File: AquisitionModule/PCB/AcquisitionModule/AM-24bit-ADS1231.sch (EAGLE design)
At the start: 4 parts, among them U1 ADS1231ID

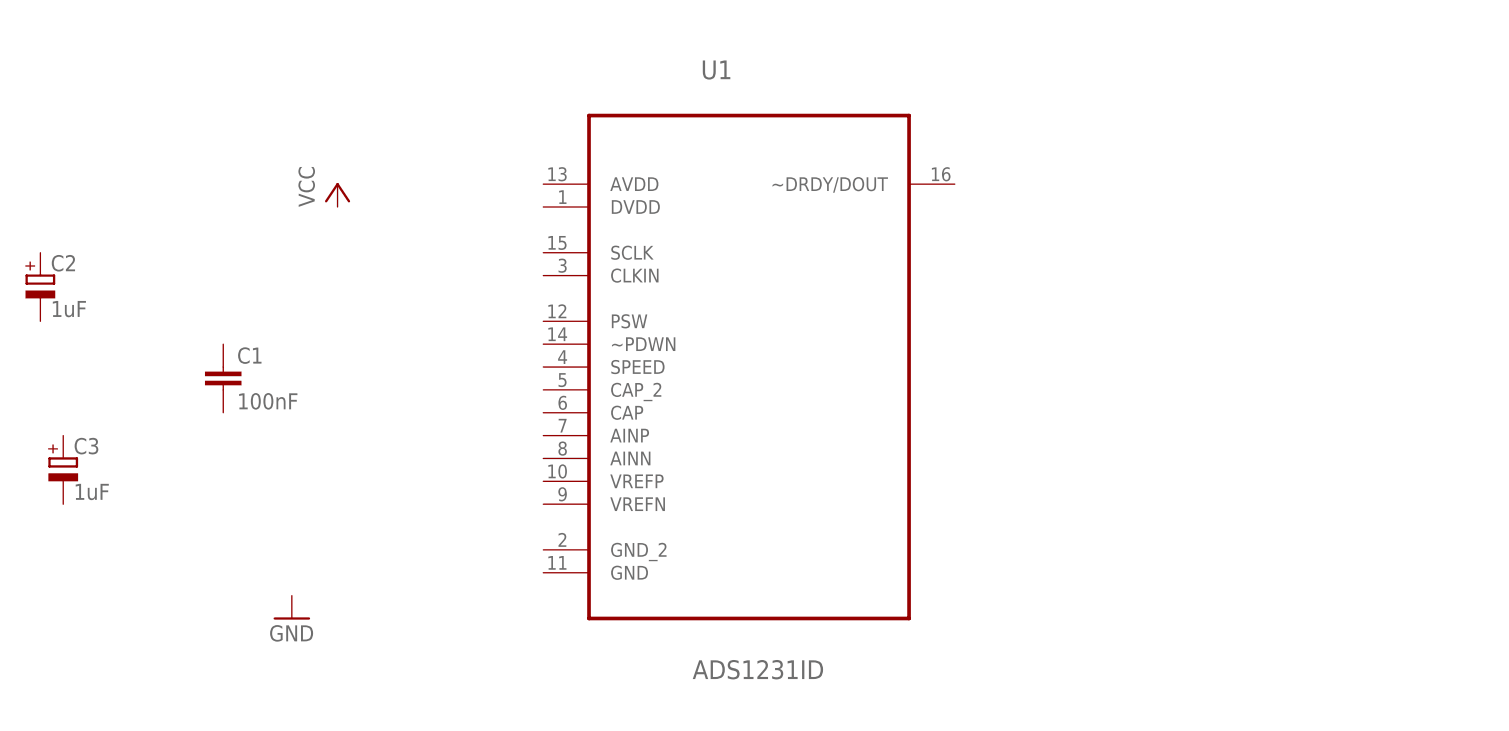
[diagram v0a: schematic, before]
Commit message: Wiring components in Acquisition Module schematic
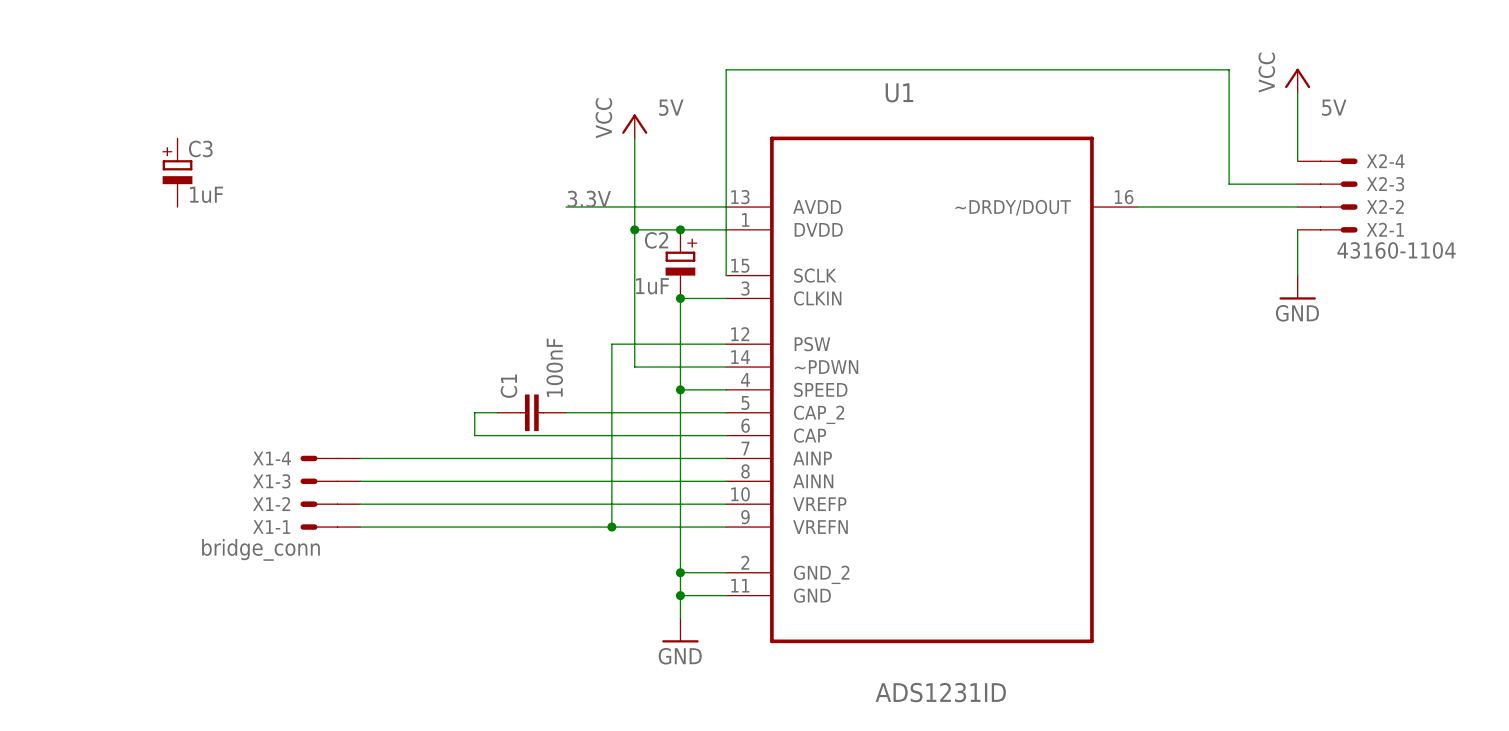
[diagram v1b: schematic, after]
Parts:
- added X1: bridge_conn, con-molex:43160-1104
- added X2: 43160-1104, con-molex:43160-1104
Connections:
- new net 3.3V: U1.AVDD
- new net 5V: C2.+, U1.DVDD, U1.~PDWN, X2-4.S@1
- new net GND: C2.-, U1.CLKIN, U1.GND, U1.GND_2, U1.SPEED, X2-1.S@1
- new net N$1: C1.2, U1.CAP_2
- new net N$2: C1.1, U1.CAP
- new net N$3: U1.PSW, U1.VREFN, X1-1.S@1
- new net N$4: U1.AINP, X1-4.S@1
- new net N$5: U1.AINN, X1-3.S@1
- new net N$6: U1.VREFP, X1-2.S@1
- new net N$7: U1.SCLK, X2-3.S@1
- new net N$8: U1.~DRDY/DOUT, X2-2.S@1
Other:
- moved on the sheet: C1, C2, C3, U1
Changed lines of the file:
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@@
 <part name="C2" library="rcl" deviceset="CPOL-EU" device="140CLH-0810" value="1uF"/>
 <part name="C3" library="rcl" deviceset="CPOL-EU" device="140CLH-0810" value="1uF"/>
-<part name="P+1" library="supply1" deviceset="VCC" device=""/>
+<part name="5V" library="supply1" deviceset="VCC" device=""/>
 <part name="GND1" library="supply1" deviceset="GND" device=""/>
+<part name="X1" library="con-molex" deviceset="43160-*04" device="" technology="11" value="bridge_conn"/>
+<part name="X2" library="con-molex" deviceset="43160-*04" device="" technology="11"/>
+<part name="5V1" library="supply1" deviceset="VCC" device=""/>
+<part name="GND2" library="supply1" deviceset="GND" device=""/>
 </parts>
 <sheets>
@@
 <instances>
 <instance part="FRAME1" gate="G$1" x="0" y="0"/>
-<instance part="U1" gate="A" x="119.38" y="96.52"/>
-<instance part="C1" gate="G$1" x="60.96" y="93.98"/>
-<instance part="C2" gate="G$1" x="40.64" y="104.14"/>
-<instance part="C3" gate="G$1" x="43.18" y="83.82"/>
-<instance part="P+1" gate="VCC" x="73.66" y="114.3"/>
-<instance part="GND1" gate="1" x="68.58" y="66.04"/>
+<instance part="U1" gate="A" x="139.7" y="93.98"/>
+<instance part="C1" gate="G$1" x="93.98" y="88.9" rot="R90"/>
+<instance part="C2" gate="G$1" x="111.76" y="106.68" rot="MR0"/>
+<instance part="C3" gate="G$1" x="55.88" y="116.84"/>
+<instance part="5V" gate="VCC" x="106.68" y="121.92"/>
+<instance part="GND1" gate="1" x="111.76" y="63.5"/>
+<instance part="X1" gate="-1" x="71.12" y="76.2" rot="R180"/>
+<instance part="X1" gate="-2" x="71.12" y="78.74" rot="R180"/>
+<instance part="X1" gate="-3" x="71.12" y="81.28" rot="R180"/>
+<instance part="X1" gate="-4" x="71.12" y="83.82" rot="R180"/>
+<instance part="X2" gate="-1" x="185.42" y="109.22" rot="MR180"/>
+<instance part="X2" gate="-2" x="185.42" y="111.76" rot="MR180"/>
+<instance part="X2" gate="-3" x="185.42" y="114.3" rot="MR180"/>
+<instance part="X2" gate="-4" x="185.42" y="116.84" rot="MR180"/>
+<instance part="5V1" gate="VCC" x="180.34" y="127"/>
+<instance part="GND2" gate="1" x="180.34" y="101.6"/>
 </instances>
 <busses>
 </busses>
 <nets>
+<net name="GND" class="0">
+<segment>
+<pinref part="U1" gate="A" pin="GND"/>
+<pinref part="GND1" gate="1" pin="GND"/>
+<wire x1="116.84" y1="68.58" x2="111.76" y2="68.58" width="0.1524" layer="91"/>
+<wire x1="111.76" y1="68.58" x2="111.76" y2="66.04" width="0.1524" layer="91"/>
+<pinref part="U1" gate="A" pin="GND_2"/>
+<wire x1="116.84" y1="71.12" x2="111.76" y2="71.12" width="0.1524" layer="91"/>
+<wire x1="111.76" y1="71.12" x2="111.76" y2="68.58" width="0.1524" layer="91"/>
+<junction x="111.76" y="68.58"/>
+<pinref part="U1" gate="A" pin="SPEED"/>
+<wire x1="116.84" y1="91.44" x2="111.76" y2="91.44" width="0.1524" layer="91"/>
+<wire x1="111.76" y1="91.44" x2="111.76" y2="71.12" width="0.1524" layer="91"/>
+<junction x="111.76" y="71.12"/>
+<junction x="111.76" y="91.44"/>
+<pinref part="U1" gate="A" pin="CLKIN"/>
+<wire x1="116.84" y1="101.6" x2="111.76" y2="101.6" width="0.1524" layer="91"/>
+<wire x1="111.76" y1="101.6" x2="111.76" y2="91.44" width="0.1524" layer="91"/>
+<pinref part="C2" gate="G$1" pin="-"/>
+<junction x="111.76" y="101.6"/>
+</segment>
+<segment>
+<pinref part="X2" gate="-1" pin="S@1"/>
+<pinref part="GND2" gate="1" pin="GND"/>
+<wire x1="180.34" y1="109.22" x2="180.34" y2="104.14" width="0.1524" layer="91"/>
+</segment>
+</net>
+<net name="N$1" class="0">
+<segment>
+<pinref part="U1" gate="A" pin="CAP_2"/>
+<pinref part="C1" gate="G$1" pin="2"/>
+<wire x1="116.84" y1="88.9" x2="99.06" y2="88.9" width="0.1524" layer="91"/>
+</segment>
+</net>
+<net name="N$2" class="0">
+<segment>
+<pinref part="C1" gate="G$1" pin="1"/>
+<wire x1="91.44" y1="88.9" x2="88.9" y2="88.9" width="0.1524" layer="91"/>
+<wire x1="88.9" y1="88.9" x2="88.9" y2="86.36" width="0.1524" layer="91"/>
+<pinref part="U1" gate="A" pin="CAP"/>
+<wire x1="88.9" y1="86.36" x2="116.84" y2="86.36" width="0.1524" layer="91"/>
+</segment>
+</net>
+<net name="5V" class="0">
+<segment>
+<pinref part="U1" gate="A" pin="DVDD"/>
+<pinref part="5V" gate="VCC" pin="VCC"/>
+<wire x1="116.84" y1="109.22" x2="111.76" y2="109.22" width="0.1524" layer="91"/>
+<wire x1="111.76" y1="109.22" x2="106.68" y2="109.22" width="0.1524" layer="91"/>
+<wire x1="106.68" y1="109.22" x2="106.68" y2="119.38" width="0.1524" layer="91"/>
+<label x="109.22" y="121.92" size="1.778" layer="95"/>
+<pinref part="U1" gate="A" pin="~PDWN"/>
+<wire x1="116.84" y1="93.98" x2="106.68" y2="93.98" width="0.1524" layer="91"/>
+<wire x1="106.68" y1="93.98" x2="106.68" y2="109.22" width="0.1524" layer="91"/>
+<junction x="106.68" y="109.22"/>
+<pinref part="C2" gate="G$1" pin="+"/>
+<junction x="111.76" y="109.22"/>
+</segment>
+<segment>
+<pinref part="X2" gate="-4" pin="S@1"/>
+<pinref part="5V1" gate="VCC" pin="VCC"/>
+<wire x1="180.34" y1="116.84" x2="180.34" y2="124.46" width="0.1524" layer="91"/>
+<label x="182.88" y="121.92" size="1.778" layer="95"/>
+</segment>
+</net>
+<net name="3.3V" class="0">
+<segment>
+<pinref part="U1" gate="A" pin="AVDD"/>
+<wire x1="116.84" y1="111.76" x2="99.06" y2="111.76" width="0.1524" layer="91"/>
+<label x="99.06" y="111.76" size="1.778" layer="95"/>
+</segment>
+</net>
+<net name="N$3" class="0">
+<segment>
+<pinref part="U1" gate="A" pin="PSW"/>
+<wire x1="116.84" y1="96.52" x2="104.14" y2="96.52" width="0.1524" layer="91"/>
+<wire x1="104.14" y1="96.52" x2="104.14" y2="76.2" width="0.1524" layer="91"/>
+<pinref part="U1" gate="A" pin="VREFN"/>
+<wire x1="104.14" y1="76.2" x2="116.84" y2="76.2" width="0.1524" layer="91"/>
+<pinref part="X1" gate="-1" pin="S@1"/>
+<wire x1="104.14" y1="76.2" x2="76.2" y2="76.2" width="0.1524" layer="91"/>
+<junction x="104.14" y="76.2"/>
+</segment>
+</net>
+<net name="N$4" class="0">
+<segment>
+<pinref part="U1" gate="A" pin="AINP"/>
+<pinref part="X1" gate="-4" pin="S@1"/>
+<wire x1="116.84" y1="83.82" x2="76.2" y2="83.82" width="0.1524" layer="91"/>
+</segment>
+</net>
+<net name="N$5" class="0">
+<segment>
+<pinref part="U1" gate="A" pin="AINN"/>
+<pinref part="X1" gate="-3" pin="S@1"/>
+<wire x1="116.84" y1="81.28" x2="76.2" y2="81.28" width="0.1524" layer="91"/>
+</segment>
+</net>
+<net name="N$6" class="0">
+<segment>
+<pinref part="U1" gate="A" pin="VREFP"/>
+<pinref part="X1" gate="-2" pin="S@1"/>
+<wire x1="116.84" y1="78.74" x2="76.2" y2="78.74" width="0.1524" layer="91"/>
+</segment>
+</net>
+<net name="N$7" class="0">
+<segment>
+<pinref part="U1" gate="A" pin="SCLK"/>
+<wire x1="116.84" y1="104.14" x2="116.84" y2="127" width="0.1524" layer="91"/>
+<wire x1="116.84" y1="127" x2="172.72" y2="127" width="0.1524" layer="91"/>
+<wire x1="172.72" y1="127" x2="172.72" y2="114.3" width="0.1524" layer="91"/>
+<pinref part="X2" gate="-3" pin="S@1"/>
+<wire x1="172.72" y1="114.3" x2="180.34" y2="114.3" width="0.1524" layer="91"/>
+</segment>
+</net>
+<net name="N$8" class="0">
+<segment>
+<pinref part="U1" gate="A" pin="~DRDY/DOUT"/>
+<wire x1="162.56" y1="111.76" x2="180.34" y2="111.76" width="0.1524" layer="91"/>
+<pinref part="X2" gate="-2" pin="S@1"/>
+</segment>
+</net>
 </nets>
 </sheet>

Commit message: Added reference voltage (2.5V) in the circuit
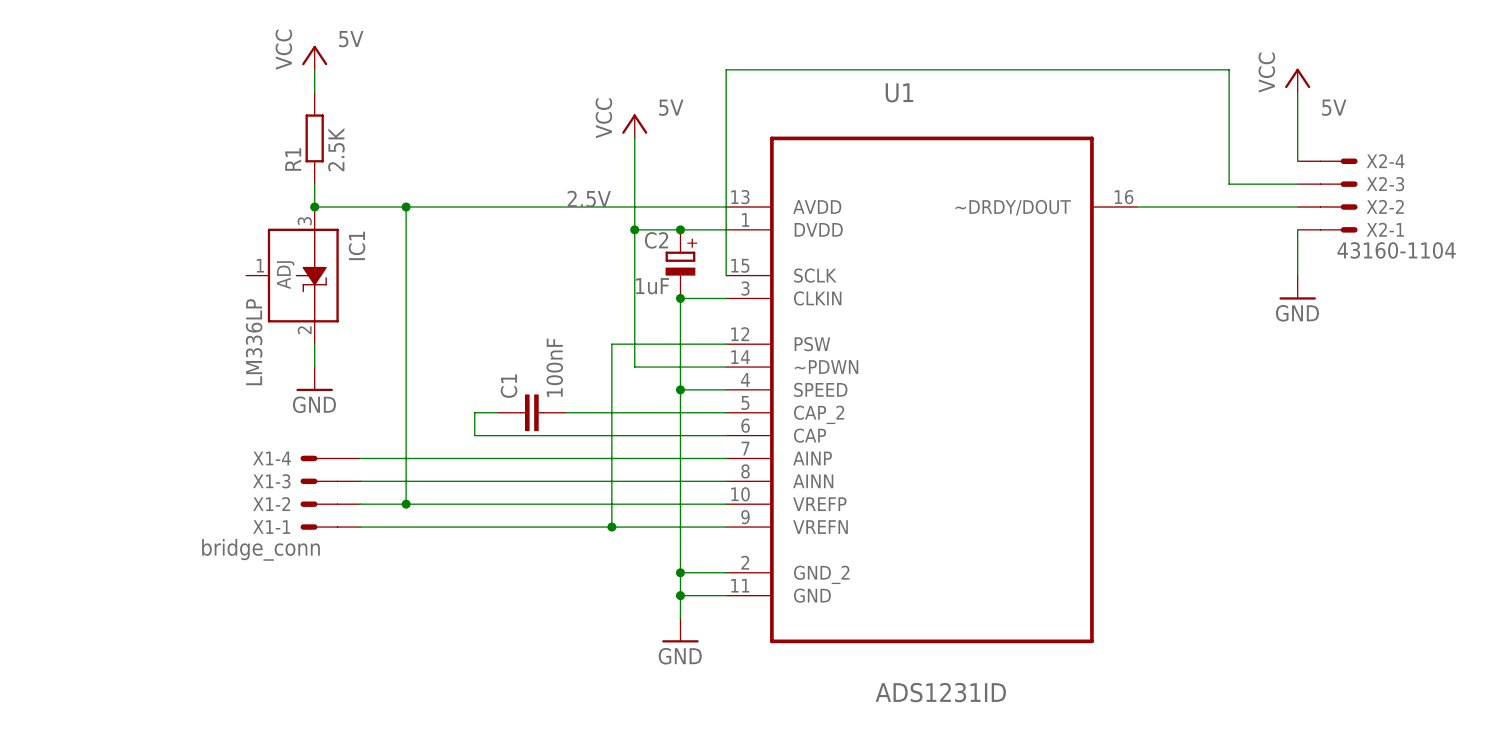
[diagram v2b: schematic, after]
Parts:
- removed C3: 1uF, rcl:CPOL-EU140CLH-0810
- added IC1: LM336LP, linear:LM336LP
- added R1: 2.5K, resistor:R-EU_R3225W
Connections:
- removed net 3.3V: U1.AVDD
- removed net N$6: U1.VREFP, X1-2.S@1
- new net 2.5V: IC1.A, R1.1, U1.AVDD, U1.VREFP, X1-2.S@1
- net 5V: now also R1.2
- net GND: now also IC1.C
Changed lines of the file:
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@@
 <part name="C1" library="rcl" deviceset="C-EU" device="C1206K" value="100nF"/>
 <part name="C2" library="rcl" deviceset="CPOL-EU" device="140CLH-0810" value="1uF"/>
-<part name="C3" library="rcl" deviceset="CPOL-EU" device="140CLH-0810" value="1uF"/>
 <part name="5V" library="supply1" deviceset="VCC" device=""/>
 <part name="GND1" library="supply1" deviceset="GND" device=""/>
@@
 <part name="5V1" library="supply1" deviceset="VCC" device=""/>
 <part name="GND2" library="supply1" deviceset="GND" device=""/>
+<part name="IC1" library="linear" deviceset="LM336" device="LP"/>
+<part name="R1" library="resistor" deviceset="R-EU_" device="R3225W" value="2.5K"/>
+<part name="GND3" library="supply1" deviceset="GND" device=""/>
+<part name="5V2" library="supply1" deviceset="VCC" device=""/>
 </parts>
 <sheets>
@@
 <instance part="C1" gate="G$1" x="93.98" y="88.9" rot="R90"/>
 <instance part="C2" gate="G$1" x="111.76" y="106.68" rot="MR0"/>
-<instance part="C3" gate="G$1" x="55.88" y="116.84"/>
 <instance part="5V" gate="VCC" x="106.68" y="121.92"/>
 <instance part="GND1" gate="1" x="111.76" y="63.5"/>
@@
 <instance part="5V1" gate="VCC" x="180.34" y="127"/>
 <instance part="GND2" gate="1" x="180.34" y="101.6"/>
+<instance part="IC1" gate="G$1" x="71.12" y="104.14" rot="R270"/>
+<instance part="R1" gate="G$1" x="71.12" y="119.38" rot="R90"/>
+<instance part="GND3" gate="1" x="71.12" y="91.44"/>
+<instance part="5V2" gate="VCC" x="71.12" y="129.54"/>
 </instances>
 <busses>
@@
 <pinref part="GND2" gate="1" pin="GND"/>
 <wire x1="180.34" y1="109.22" x2="180.34" y2="104.14" width="0.1524" layer="91"/>
+</segment>
+<segment>
+<pinref part="IC1" gate="G$1" pin="C"/>
+<pinref part="GND3" gate="1" pin="GND"/>
+<wire x1="71.12" y1="96.52" x2="71.12" y2="93.98" width="0.1524" layer="91"/>
 </segment>
 </net>
@@
 <label x="182.88" y="121.92" size="1.778" layer="95"/>
 </segment>
+<segment>
+<pinref part="5V2" gate="VCC" pin="VCC"/>
+<pinref part="R1" gate="G$1" pin="2"/>
+<wire x1="71.12" y1="127" x2="71.12" y2="124.46" width="0.1524" layer="91"/>
+<label x="73.66" y="129.54" size="1.778" layer="95"/>
+</segment>
 </net>
-<net name="3.3V" class="0">
+<net name="2.5V" class="0">
 <segment>
 <pinref part="U1" gate="A" pin="AVDD"/>
-<wire x1="116.84" y1="111.76" x2="99.06" y2="111.76" width="0.1524" layer="91"/>
 <label x="99.06" y="111.76" size="1.778" layer="95"/>
+<pinref part="R1" gate="G$1" pin="1"/>
+<pinref part="IC1" gate="G$1" pin="A"/>
+<wire x1="71.12" y1="114.3" x2="71.12" y2="111.76" width="0.1524" layer="91"/>
+<wire x1="116.84" y1="111.76" x2="81.28" y2="111.76" width="0.1524" layer="91"/>
+<junction x="71.12" y="111.76"/>
+<pinref part="U1" gate="A" pin="VREFP"/>
+<pinref part="X1" gate="-2" pin="S@1"/>
+<wire x1="81.28" y1="111.76" x2="71.12" y2="111.76" width="0.1524" layer="91"/>
+<wire x1="116.84" y1="78.74" x2="81.28" y2="78.74" width="0.1524" layer="91"/>
+<wire x1="81.28" y1="78.74" x2="76.2" y2="78.74" width="0.1524" layer="91"/>
+<wire x1="81.28" y1="78.74" x2="81.28" y2="111.76" width="0.1524" layer="91"/>
+<junction x="81.28" y="111.76"/>
+<junction x="81.28" y="78.74"/>
 </segment>
 </net>
@@
 </segment>
 </net>
-<net name="N$6" class="0">
-<segment>
-<pinref part="U1" gate="A" pin="VREFP"/>
-<pinref part="X1" gate="-2" pin="S@1"/>
-<wire x1="116.84" y1="78.74" x2="76.2" y2="78.74" width="0.1524" layer="91"/>
-</segment>
-</net>
